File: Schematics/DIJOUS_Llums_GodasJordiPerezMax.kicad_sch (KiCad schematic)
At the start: 99 parts, among them J1 Conn_01x03, J2 Conn_01x06, J3 Screw_Terminal_01x02, J4 Conn_01x05_Socket, J5 Conn_01x05, J6 DE9_Plug, J7 Conn_01x02, J8 Conn_01x06_Socket, K1 G5LE-1 DC12, K2 G5LE-1 DC12, Q1 ZXTN19020DFFTA, Q2 ZXTN19020DFFTA, Q3 ZXTN19020DFFTA, Q4 Si7336ADP, Q5 Si7336ADP, Q6 ZXTN19020DFFTA, Q7 ZXTN19020DFFTA, Q8 Si7336ADP, Q9 Si7336ADP, U1 PCA9306D, U2 PIC18F2580-I/SO, U3 LM2596T-ADJ, U4 MCP2551-I-SN, U5 ADP7112ACBZ-3.3-R7, U6 ADM7172ACPZ-5.0-R7, U7 LT6202CS5

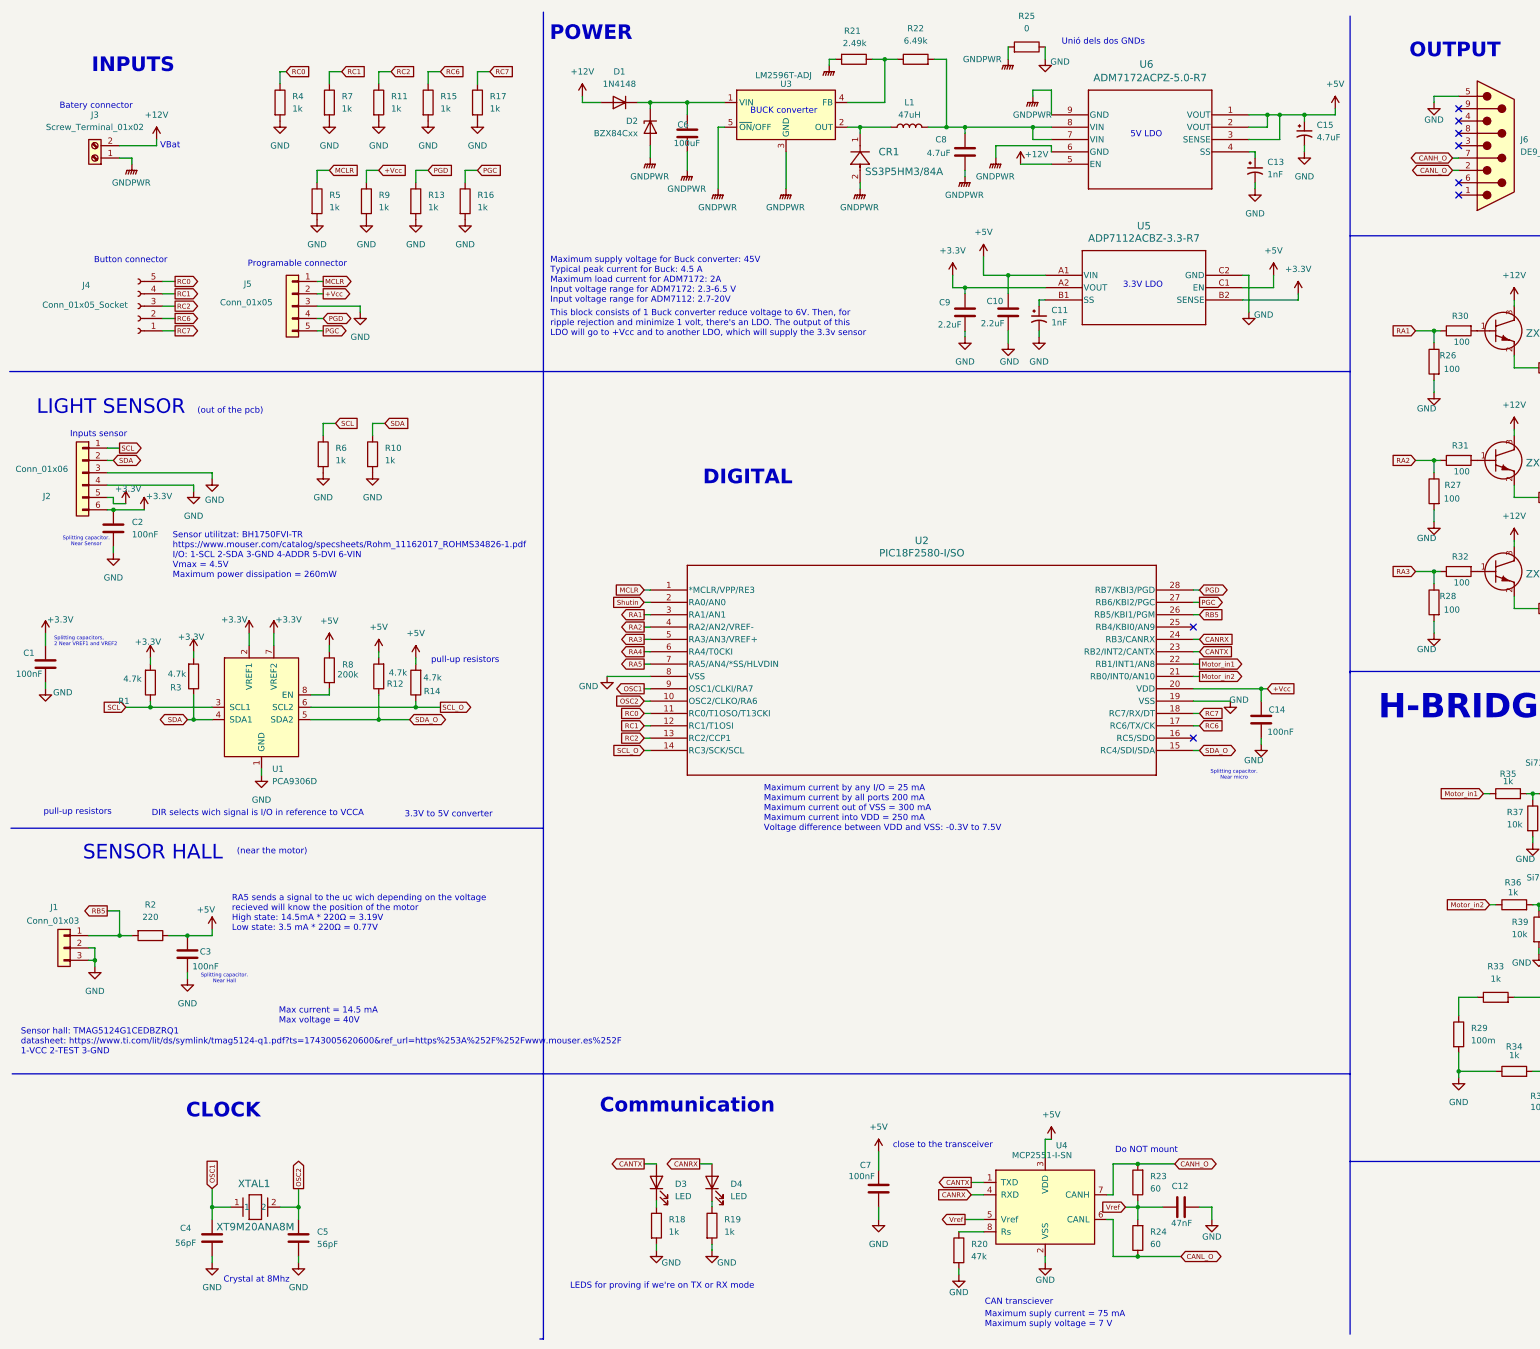
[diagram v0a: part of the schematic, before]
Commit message: Update DIJOUS_Llums_GodasJordiPerezMax.kicad_sch
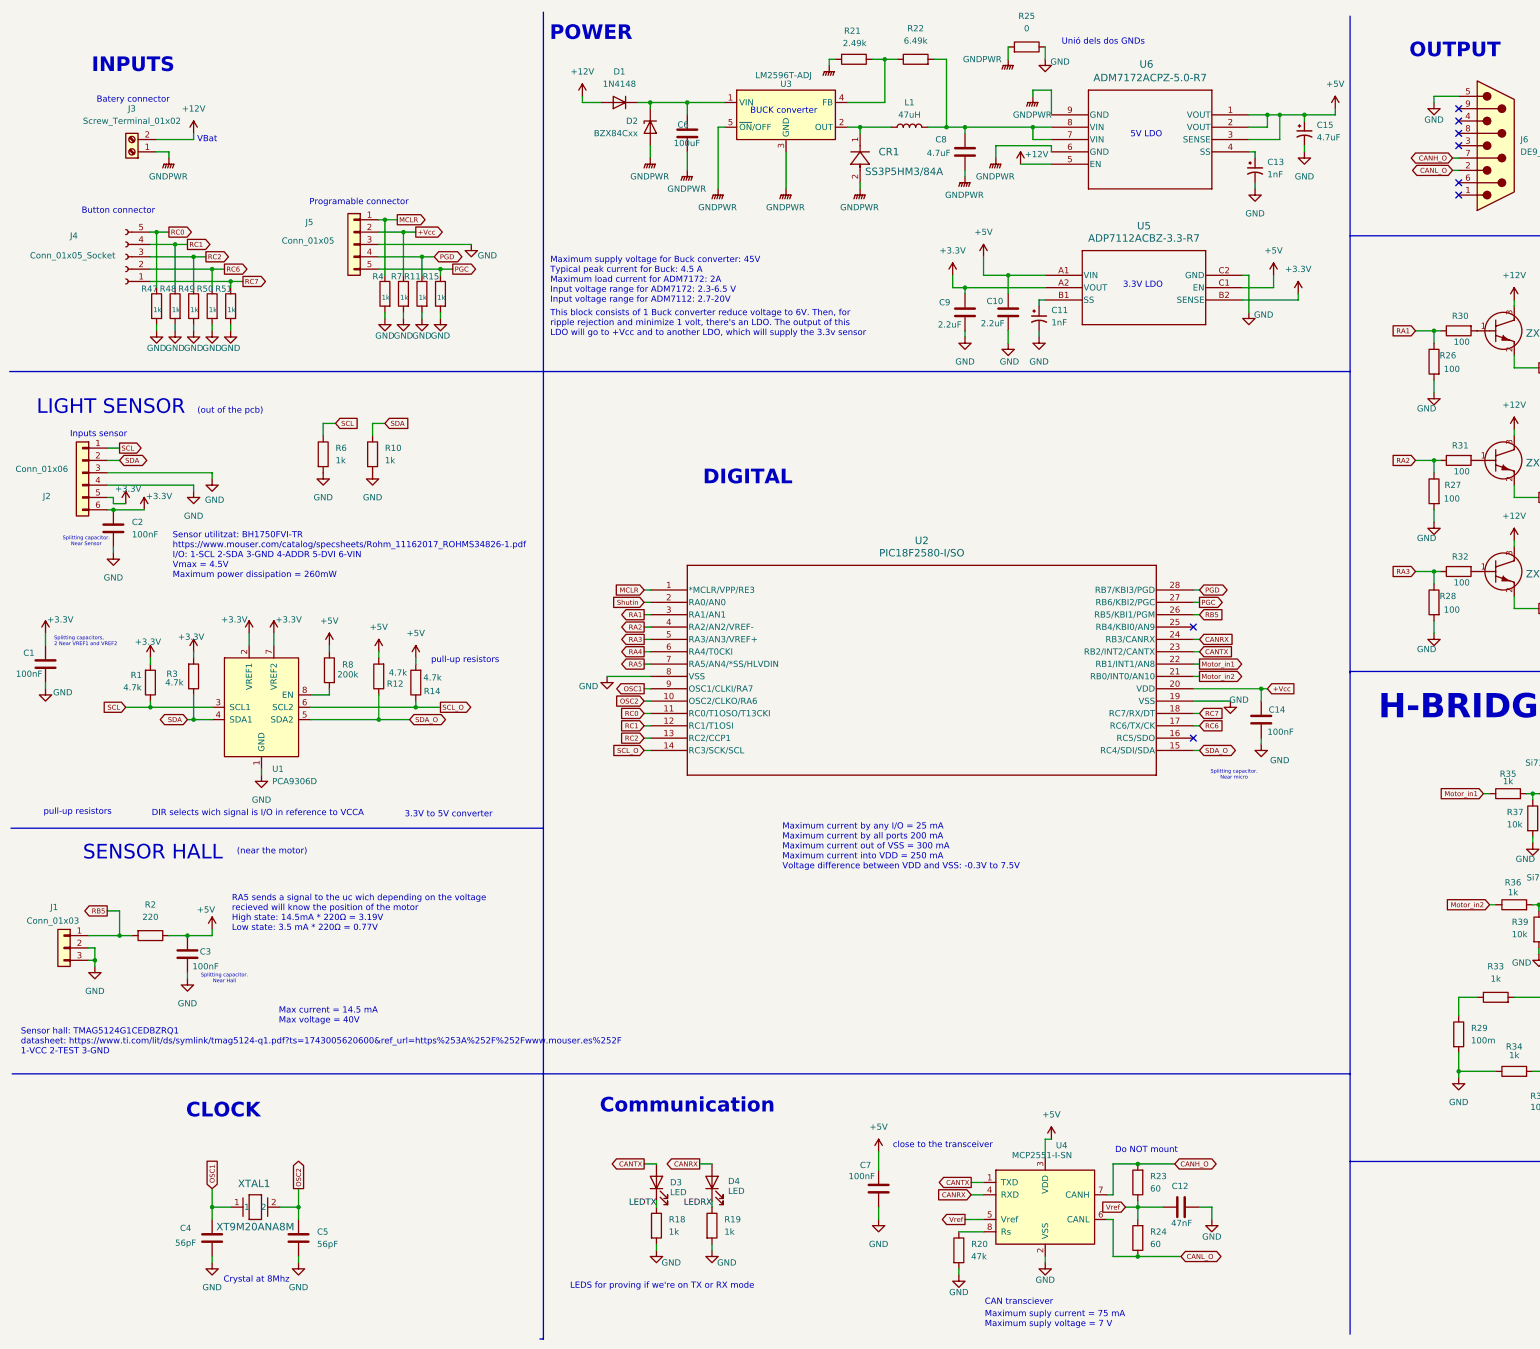
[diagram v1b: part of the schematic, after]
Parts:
- removed R13, R16, R17, R5, R9: 1k, Resistor_SMD:R_1206_3216Metric, symbol Device:R
- added R47, R48, R49, R50, R51: 1k, Resistor_SMD:R_1206_3216Metric, symbol Device:R
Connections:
- net +Vcc: now also R7.1
- net GND: now also R47.2, R48.2, R49.2, R50.2, R51.2
- net MCLR: now also R4.1
- net PGC: now also R15.1
- net PGD: now also R11.1
- net RC0: now also R47.1; no longer R4.1
- net RC1: now also R48.1; no longer R7.1
- net RC2: now also R49.1; no longer R11.1
- net RC6: now also R50.1; no longer R15.1
- net RC7: now also R51.1
- net LEDTX: now reaches D3.1 (K), R18.1
- net LEDRX: now reaches D4.1 (K), R19.1
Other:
- moved on the sheet: J3, J4, J5

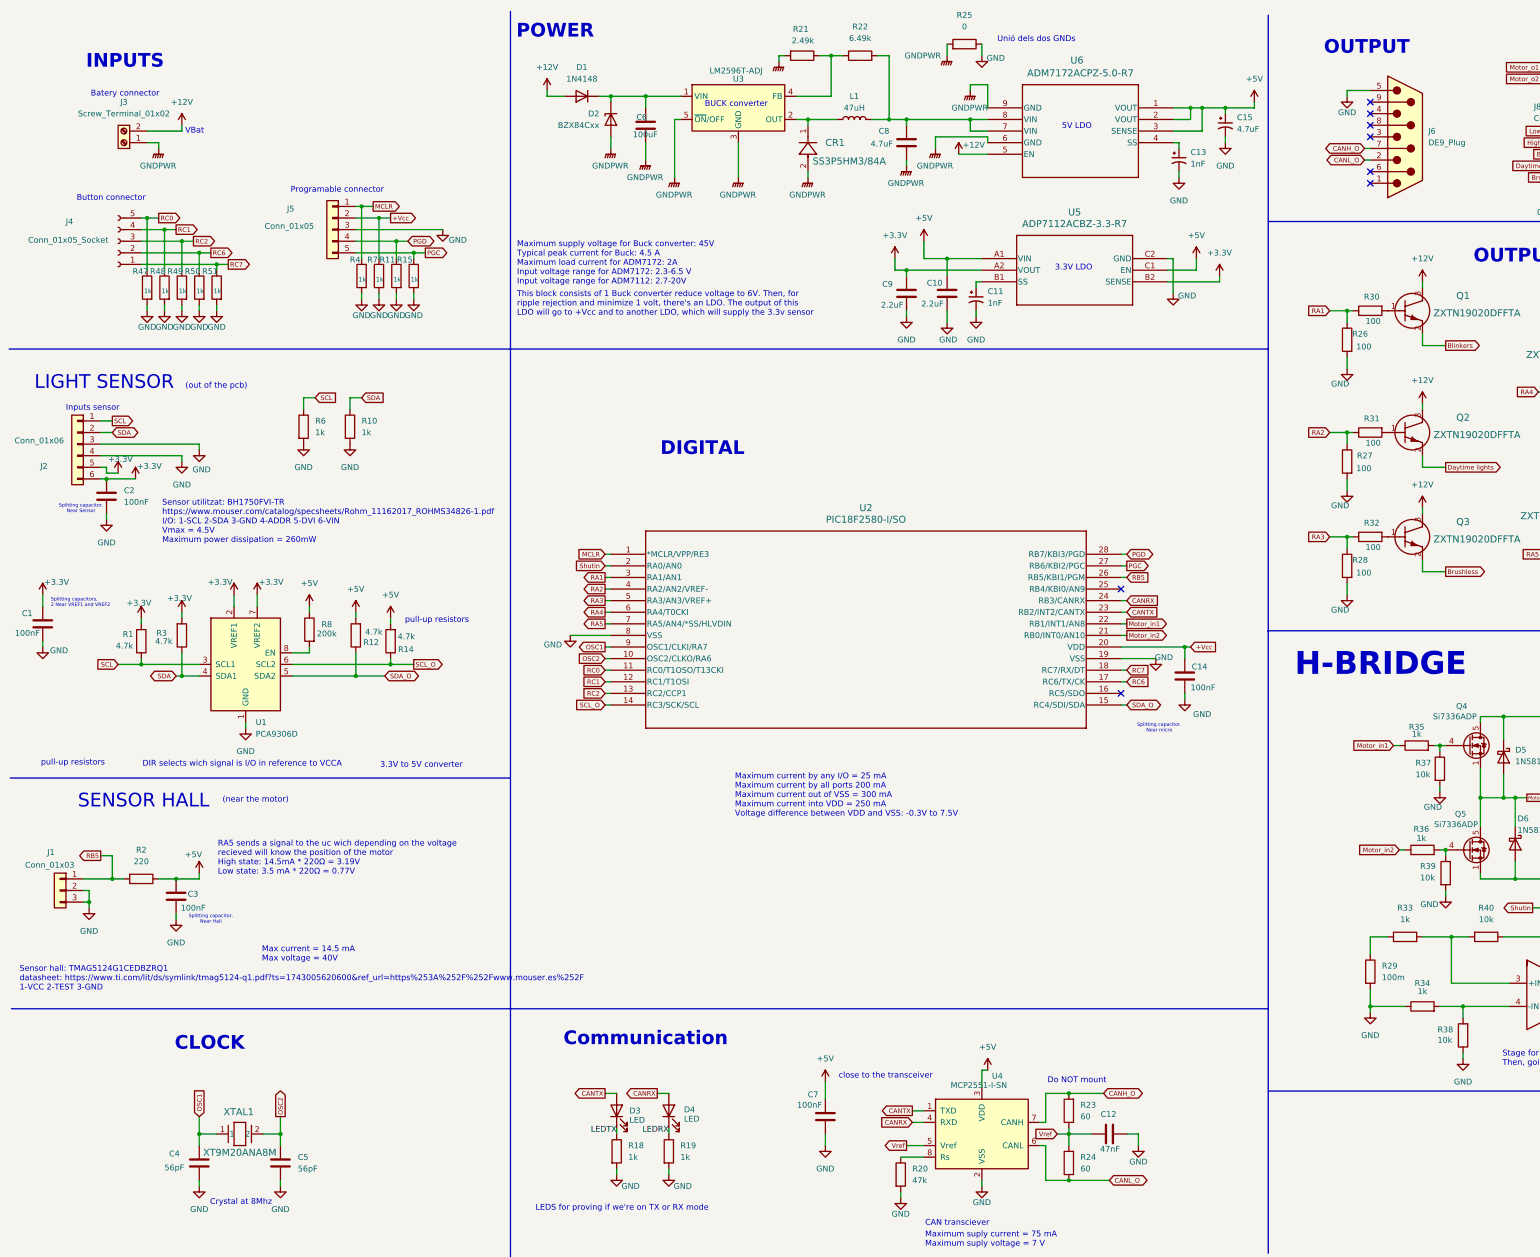
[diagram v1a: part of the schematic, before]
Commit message: Update DIJOUS_Llums_GodasJordiPerezMax.kicad_sch
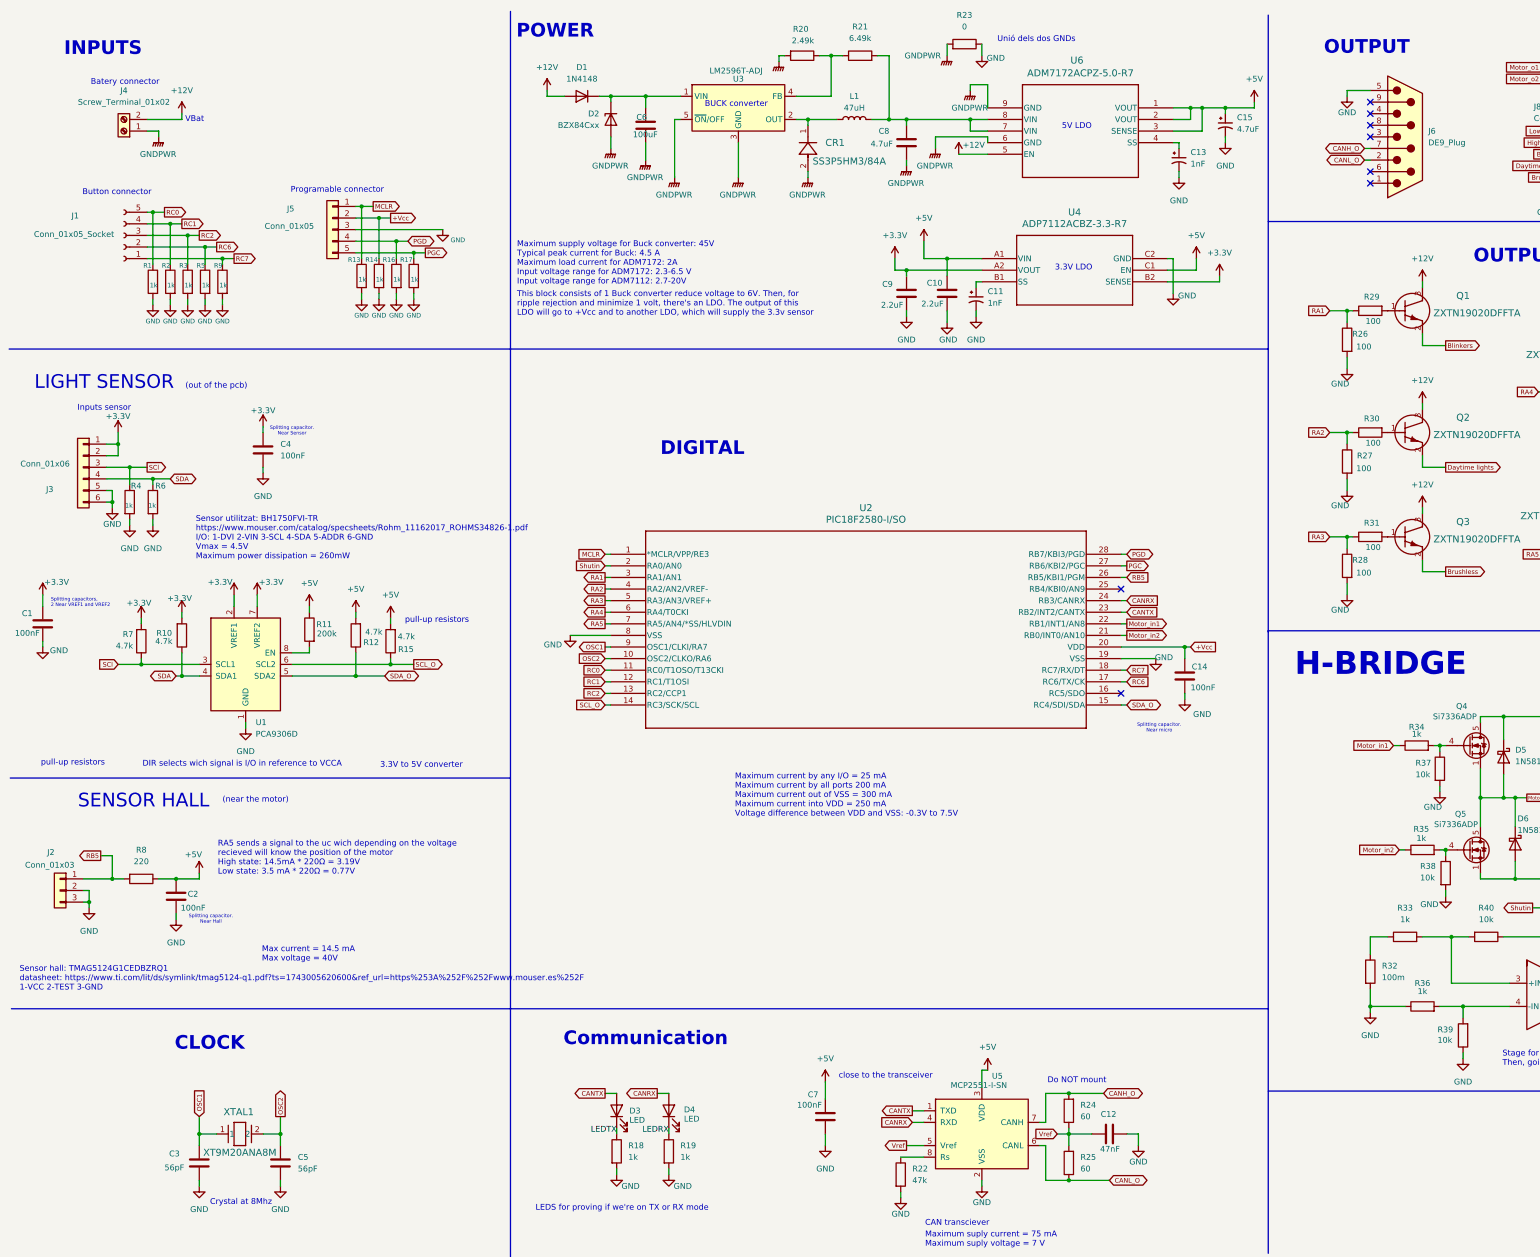
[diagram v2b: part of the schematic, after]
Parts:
- removed C2: 100nF, Capacitor_SMD:C_1206_3216Metric_Pad1.33x1.80mm_HandSolder, symbol Device:C
- removed J2: Conn_01x06, Connector_PinHeader_1.00mm:PinHeader_1x06_P1.00mm_Vertical, symbol Connector_Generic:Conn_01x06
- removed R10: 1k, Resistor_SMD:R_1206_3216Metric, symbol Device:R
- added C4: 100nF, Capacitor_SMD:C_1206_3216Metric_Pad1.33x1.80mm_HandSolder, symbol Device:C
- added J3: Conn_01x06, Connector_PinHeader_1.00mm:PinHeader_1x06_P1.00mm_Vertical, symbol Connector_Generic:Conn_01x06
- added R4: 1k, Resistor_SMD:R_1206_3216Metric, symbol Device:R
- renumbered C3 to C2, C4 to C3, J4 to J1, J1 to J2, J3 to J4, R47 to R1, R3 to R10, R8 to R11, R4 to R13, R7 to R14, R14 to R15, R11 to R16, R15 to R17, R48 to R2, R21 to R20, R22 to R21, R20 to R22, R25 to R23, R23 to R24, R24 to R25, R30 to R29, R49 to R3, R31 to R30, R32 to R31, R29 to R32, R35 to R34, R36 to R35, R34 to R36, R39 to R38, R38 to R39, R50 to R5, R1 to R7, R2 to R8, R51 to R9, U5 to U4, U4 to U5
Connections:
- net +3.3V: now also C4.1, J3.1 (Pin_1), J3.2 (Pin_2)
- net GND: now also C4.2, J3.5 (Pin_5), J3.6 (Pin_6), R4.2
- net SDA: now also R6.1, J3.4 (Pin_4)
- net SCL renamed SCl
- net SCl: now also J3.3 (Pin_3), R4.1; no longer R6.1
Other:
- note added: "Sensor utilitzat: BH1750FVI-TR https://www.mouser.com/catalog/specsheets/Rohm_11162017_ROHMS34826-1.pdf I/O: 1-DVI 2-VIN 3-SCL 4-SDA 5-ADDR 6-GND Vmax = 4.5V Maximum power dissipation = 260mW"
- note removed: "Sensor utilitzat: BH1750FVI-TR https://www.mouser.com/catalog/specsheets/Rohm_11162017_ROHMS34826-1.pdf I/O: 1-SCL 2-SDA 3-GND 4-ADDR 5-DVI 6-VIN Vmax = 4.5V Maximum power dissipation = 260mW"
- moved on the sheet: J1, J4, R1, R2, R3, R5, R9

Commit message: Update DIJOUS_Llums_GodasJordiPerezMax.kicad_sch
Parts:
- added C17: 100nF, Capacitor_SMD:C_1206_3216Metric_Pad1.33x1.80mm_HandSolder, symbol Device:C
- added R47: 100, Resistor_SMD:R_1206_3216Metric, symbol Device:R
- C12: footprint Capacitor_SMD:C_1206_3216Metric_Pad1.33x1.80mm_HandSolder -> (none)
- J4: footprint Connector_PinHeader_1.00mm:PinHeader_1x02_P1.00mm_Horizontal -> Connector_PinHeader_1.00mm:PinHeader_1x02_P1.00mm_Vertical
- R14: value 1k -> 100
- R24, R25: footprint Resistor_THT:R_Axial_DIN0204_L3.6mm_D1.6mm_P5.08mm_Horizontal -> (none)
- U4: footprint ADP7112ACBZ-3.3-R7:CB-6-15_ADI -> ADP7112ACBZ-3.3-R7:CB-6-15_ADI-M
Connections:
- net +3.3V: no longer U1.7 (VREF2)
- net +5V: now also C14.1, J5.2 (Pin_2), U1.7 (VREF2), U2.20 (VDD), C17.2
- net GND: now also C17.1; no longer R14.2
- net RA4: now also R14.1; no longer Q6.1
- net RA5: now also R47.1; no longer Q7.1
- net BJTbase12: now reaches Q8.4 (G), R43.1, R45.1
- net BJTbase11: now reaches Q4.4 (G), R34.2, R37.1
- net BJTbase22: now reaches Q9.4 (G), R44.1, R46.1
- net BJTbase21: now reaches Q5.4 (G), R35.2, R38.1
- removed net +Vcc: C14.1, J5.2 (Pin_2), R14.1, U2.20 (VDD)
- new net: Q6.1, R14.2
- new net: Q7.1, R47.2
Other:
- note added: "Splitting capacitors, Near VREF1 and VREF2"
- note removed: "Splitting capacitors, 2 Near VREF1 and VREF2"
- moved on the sheet: C1, K1, K2, Q6, Q7, R10, R11, R12, R15, R26, R27, R28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
